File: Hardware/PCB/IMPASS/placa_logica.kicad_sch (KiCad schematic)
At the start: 32 parts, among them J17 PUENTE H_1, J18 PUENTE H_2, J19 SOLENOIDES, J20 SENSORES, J21 PROG, Q67 2N7002, Q68 2N7002, Q69 2N7002, SW1 RESET, SW2 BOOT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

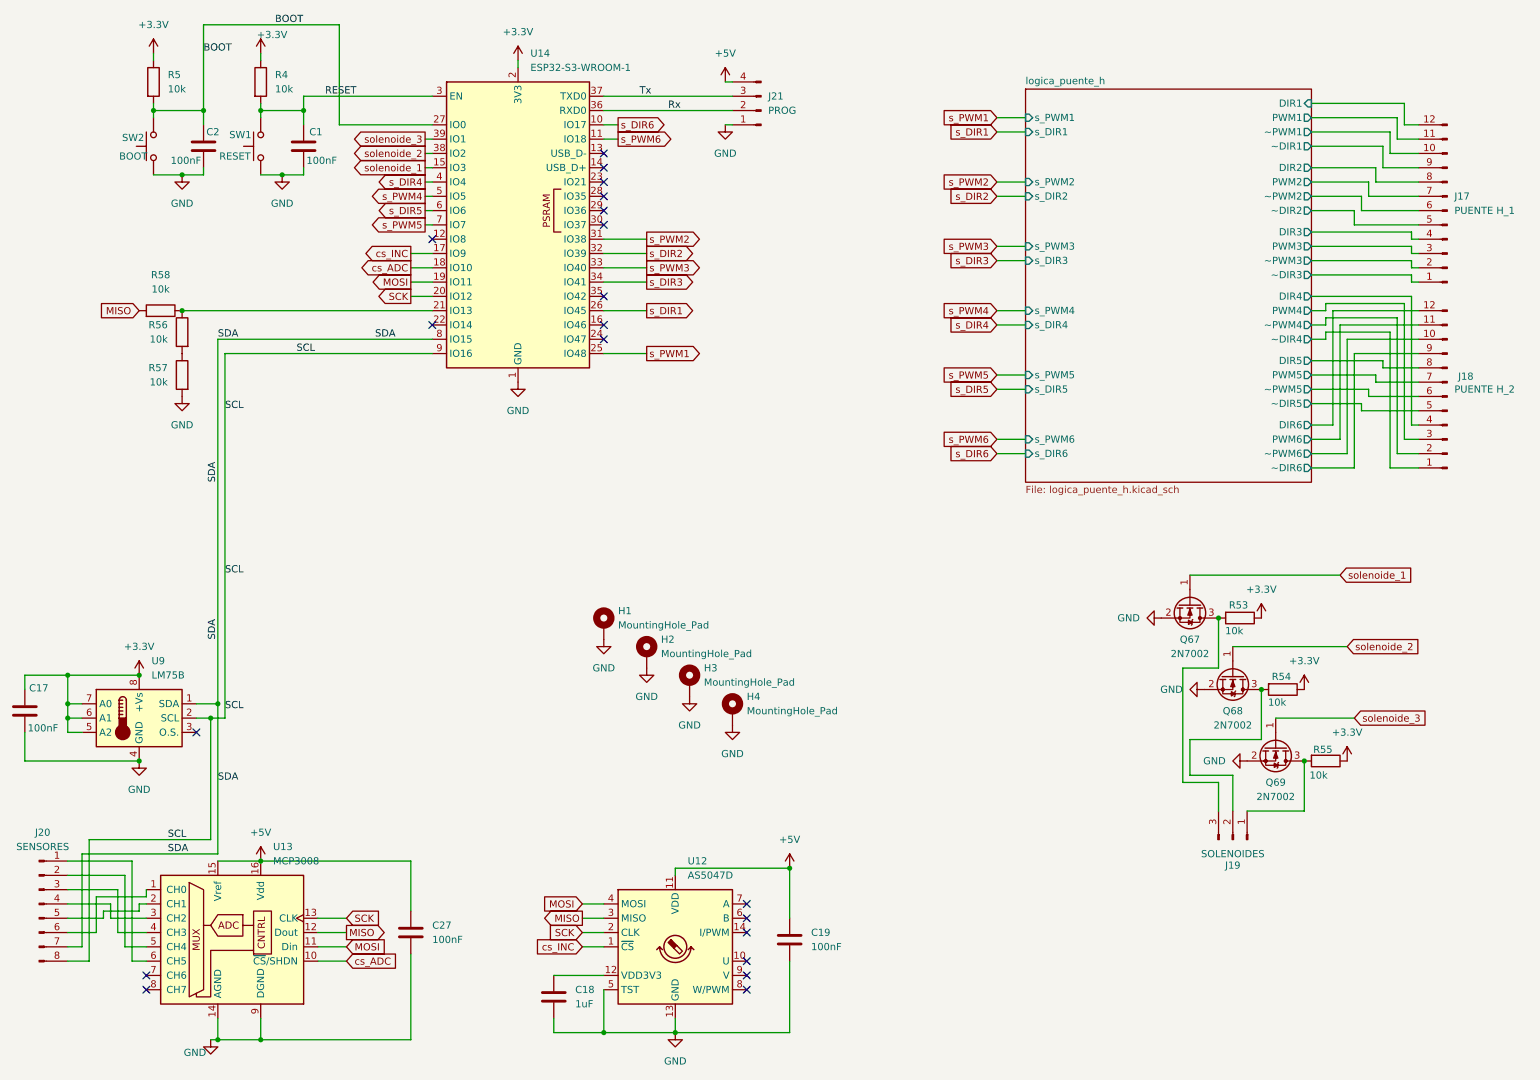
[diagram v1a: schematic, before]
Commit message: Hardware: update schematic and PCB layout 	- Replace the LDOs with buck converters 	- Replace AD5047D with LIS3DH
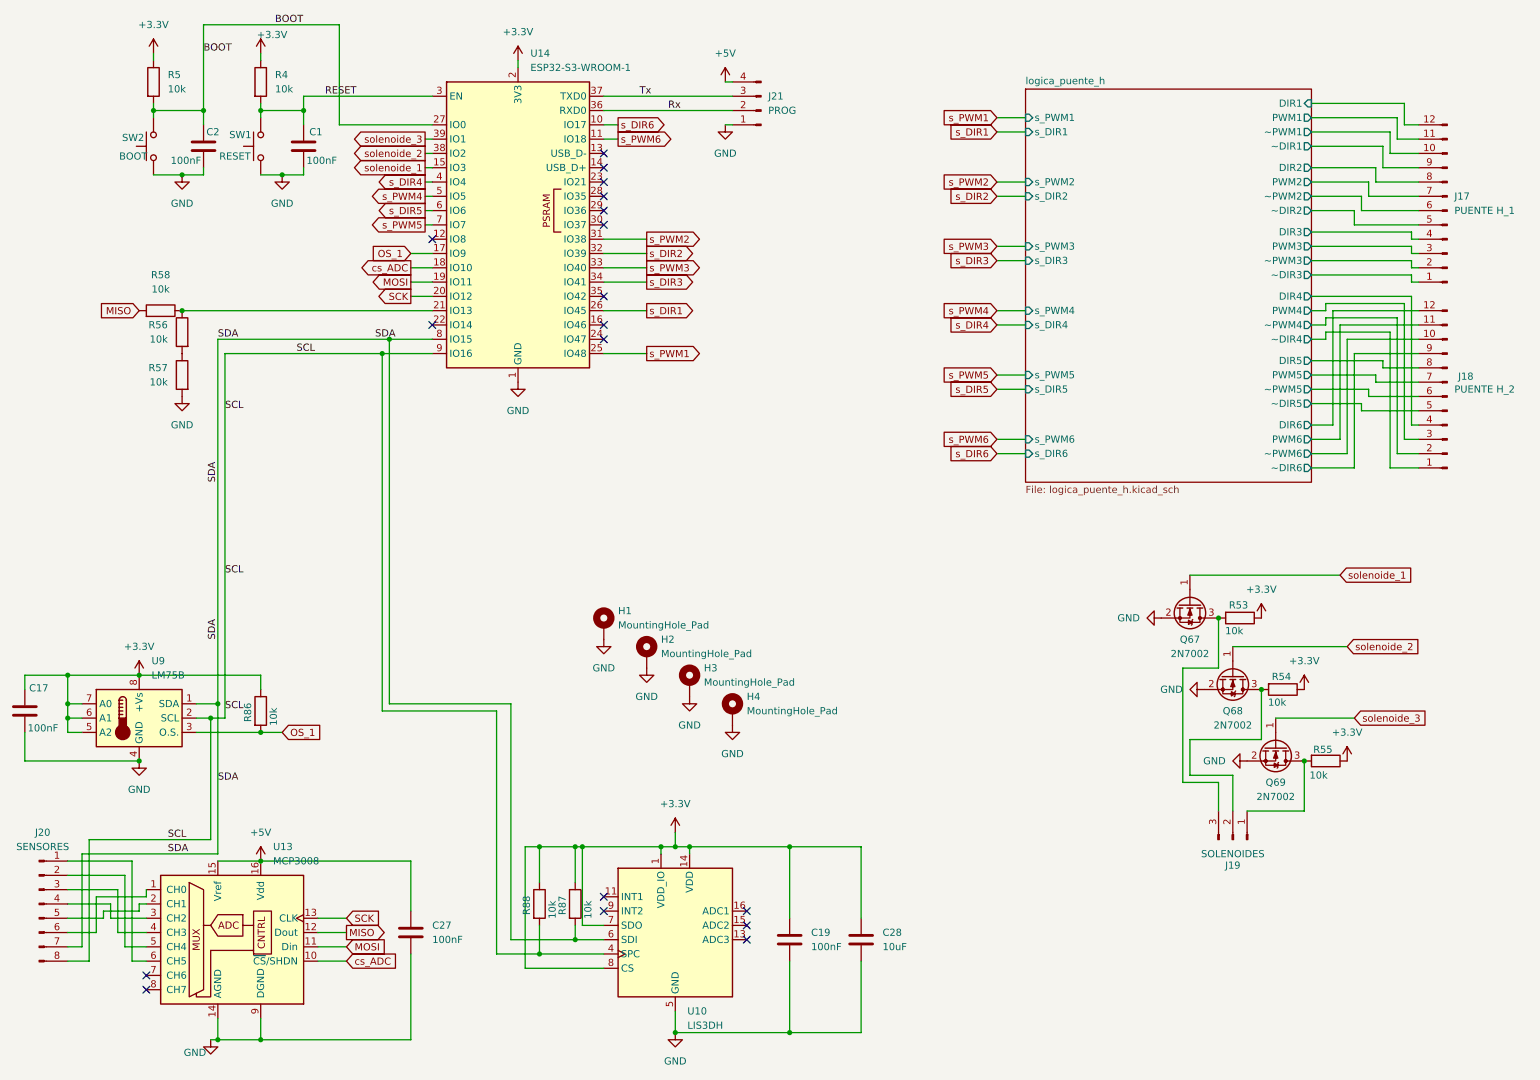
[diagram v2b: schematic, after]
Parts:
- removed C18: 1uF, Capacitor_SMD:C_0603_1608Metric, symbol Device:C
- removed U12: AS5047D, Package_SO:TSSOP-14_4.4x5mm_P0.65mm, symbol Sensor_Magnetic:AS5047D
- added C28: 10uF, Capacitor_SMD:C_0603_1608Metric, symbol Device:C
- added R86, R87, R88: 10k, Resistor_SMD:R_0603_1608Metric, symbol Device:R
- added U10: LIS3DH, Package_LGA:LGA-16_3x3mm_P0.5mm_LayoutBorder3x5y, symbol Sensor_Motion:LIS3DH
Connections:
- net cs_INC is gone; now on net OS_1: U14.17 (IO9)
- net +3.3V: now also C19.1, C28.1, R86.1, R87.1, R88.1, U10.1 (VDD_IO), U10.14 (VDD), U10.7 (SDO), U10.8 (CS)
- net +5V: no longer C19.1
- net GND: now also C28.2, U10.10 (GND), U10.12 (GND), U10.5 (GND)
- net SCL: now also R88.2, U10.4 (SPC)
- net SDA: now also R87.2, U10.6 (SDI)
- net OS_1: now reaches U9.3 (O.S.)
- net OS_1: now also R86.2
- no-connect marks 20 -> 18
